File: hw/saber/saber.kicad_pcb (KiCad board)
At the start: 4 copper layers, 62.6 x 28.2 mm, 80 parts, among them J1 282834-2, J2 282834-2, J3 OSTVN12A150, J4 NUCLEO144ZE-STLINK, Q1 STL120N4F6AG, Q2 SIS413DN-T1-GE3, Q3 SSM3K337R, Q4 STL76DN4LF7AG, Q5 SSM3K337R, Q6 SSM3K337R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

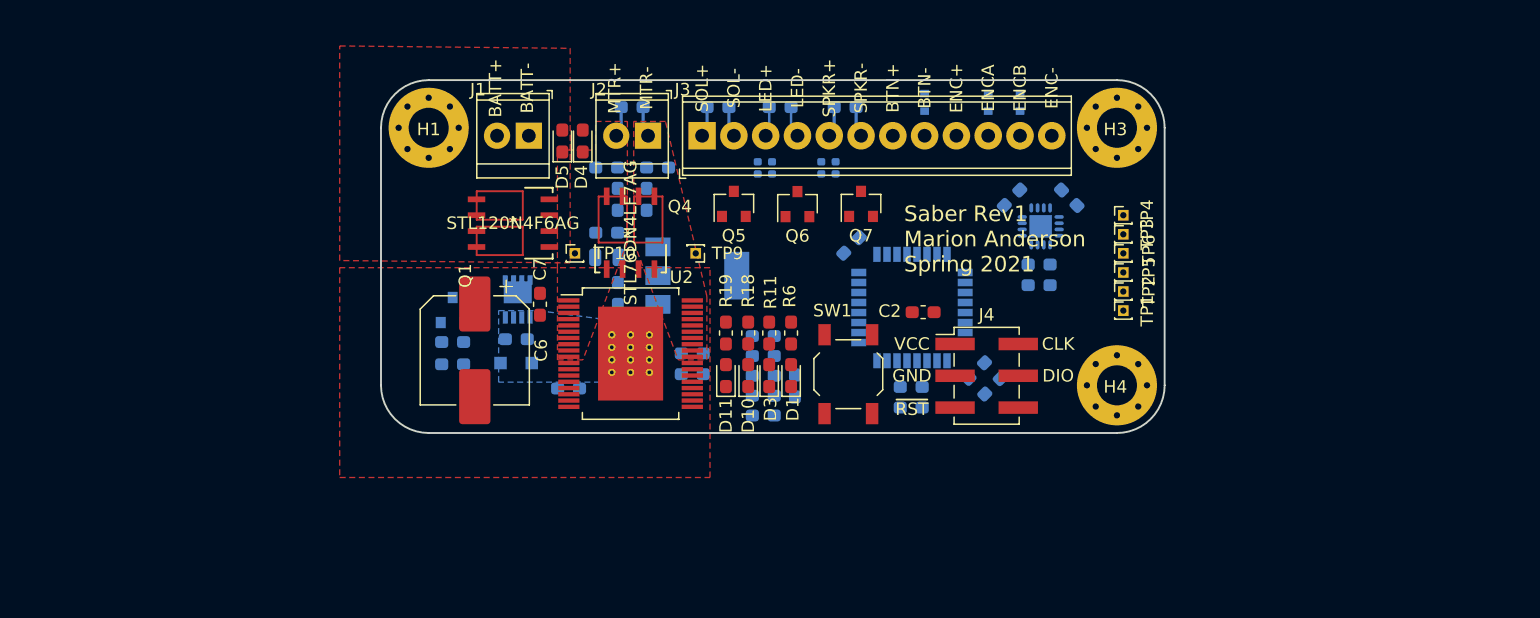
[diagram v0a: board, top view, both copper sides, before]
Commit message: more shrinking layout
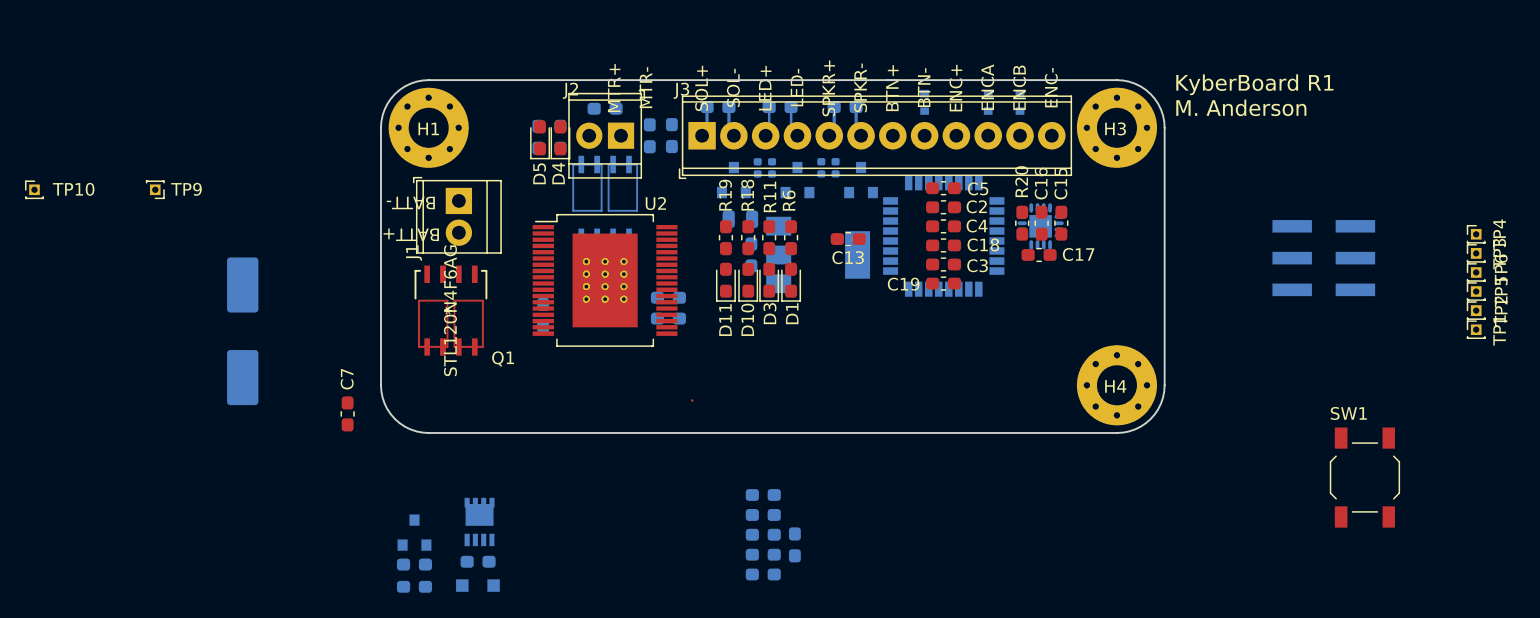
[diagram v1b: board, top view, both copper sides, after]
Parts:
- C13, C15, C16, C17, C18, C19, C3, C4, C5, R20: moved to F.Cu
- C6, J4, Q4, Q5, Q6, Q7: moved to B.Cu
- moved TP9 43.5 mm to (96.4, 76.1)
- moved TP10 43.5 mm to (86.7, 76.1)
- moved SW1 42.1 mm to (193.0, 99.1)
- moved J4 28.5 mm to (189.8, 81.5)
- moved TP1 28.2 mm to (201.9, 87.2)
- moved TP2 28.2 mm to (201.9, 85.7)
- moved TP3 28.2 mm to (201.9, 81.2)
- moved TP4 28.2 mm to (201.9, 79.6)
- moved TP5 28.2 mm to (201.9, 84.2)
- moved TP6 28.2 mm to (201.9, 82.7)
- moved C13 18.9 mm to (151.8, 80.0), turned to 180 degrees
- moved C6 18.6 mm to (103.4, 87.4), turned to 90 degrees
- moved Q2 18.0 mm to (122.3, 102.6)
- moved R10 18.0 mm to (117.1, 106.0)
- moved R9 18.0 mm to (117.1, 107.8)
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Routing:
- net /MOT-: track 2.97 -> 0.00 mm
- net /MOT+: track 2.61 -> 0.00 mm
- removed copper zone on F.Cu, net /BATT+
- removed copper zone on F.Cu, net /MOT+
- removed copper zone on F.Cu, net /MOT-
- removed copper zone on B.Cu, net /hbridge/VCC
- removed copper zone on F.Cu, net /hbridge/VCC
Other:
- board text added: "KyberBoard R1 M. Anderson"
- board text removed: "Saber Rev1 Marion Anderson Spring 2021"

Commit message: Maximum density placement. Next: Tidy for routing + minor footprint corrections
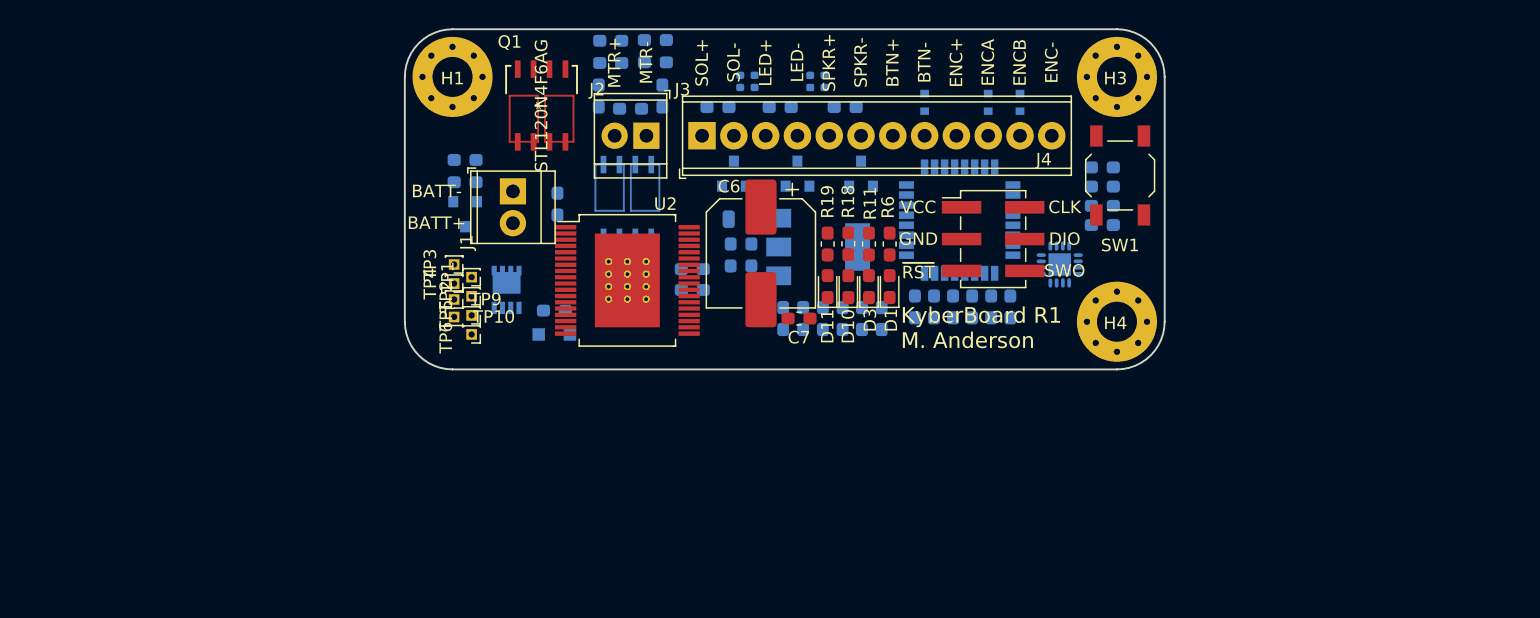
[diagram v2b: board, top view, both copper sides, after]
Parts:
- C13, C15, C16, C17, C18, C19, C2, C3, C4, C5, D4, D5, R20: moved to B.Cu
- C6, J4: moved to F.Cu
- moved TP4 81.8 mm to (120.3, 83.6), turned to 180 degrees
- moved TP3 81.7 mm to (120.3, 82.0), turned to 180 degrees
- moved TP6 80.4 mm to (121.7, 87.6), turned to 180 degrees
- moved TP1 80.4 mm to (121.7, 83.1), turned to 180 degrees
- moved TP5 80.3 mm to (121.7, 86.1), turned to 180 degrees
- moved TP2 80.3 mm to (121.7, 84.6), turned to 180 degrees
- moved C6 41.9 mm to (144.8, 81.2), turned to 270 degrees
- moved C7 36.9 mm to (147.8, 86.4), turned to 180 degrees
- moved TP10 35.0 mm to (120.3, 86.2)
- moved R9 34.3 mm to (121.1, 73.7), turned to 180 degrees
- moved SW1 31.1 mm to (173.5, 74.9), turned to 90 degrees
- moved R10 30.8 mm to (121.1, 75.5), turned to 180 degrees
- moved J4 26.5 mm to (163.3, 80.0)
- moved Q3 25.8 mm to (121.1, 78.0), turned to 270 degrees
- moved TP9 25.4 mm to (120.3, 84.8)
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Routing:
- net /LED+: track 4.02 -> 2.02 mm
- net /SPKR-: track 2.45 -> 0.56 mm
- net /SPKR+: track 4.07 -> 2.18 mm
- net /SOL-: track 2.45 -> 0.56 mm
- net +12V: track 2.45 -> 0.56 mm
- net /LED-: track 2.50 -> 0.72 mm
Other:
- board size 62.6 x 28.2 mm -> 60.7 x 27.2 mm
- board text added: "SWO"

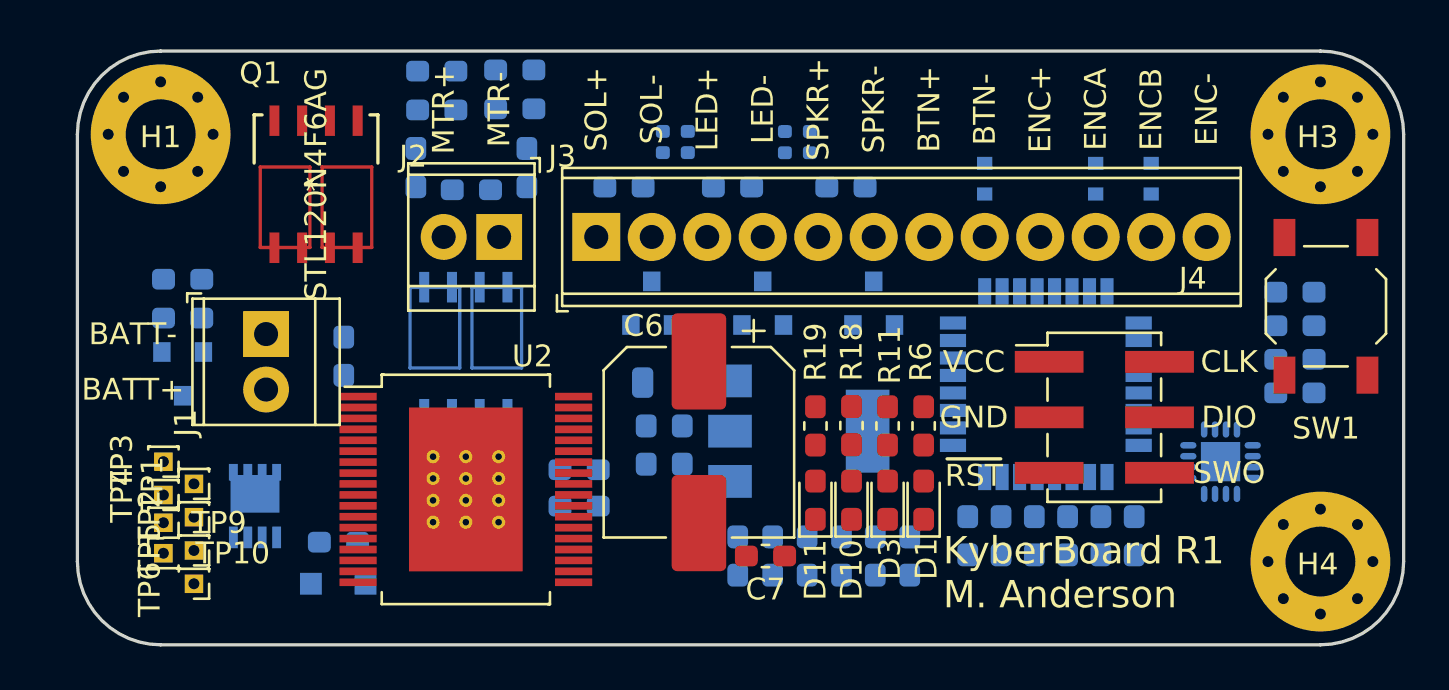
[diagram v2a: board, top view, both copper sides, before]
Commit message: correct weird pad for STL76DN4LF7AG
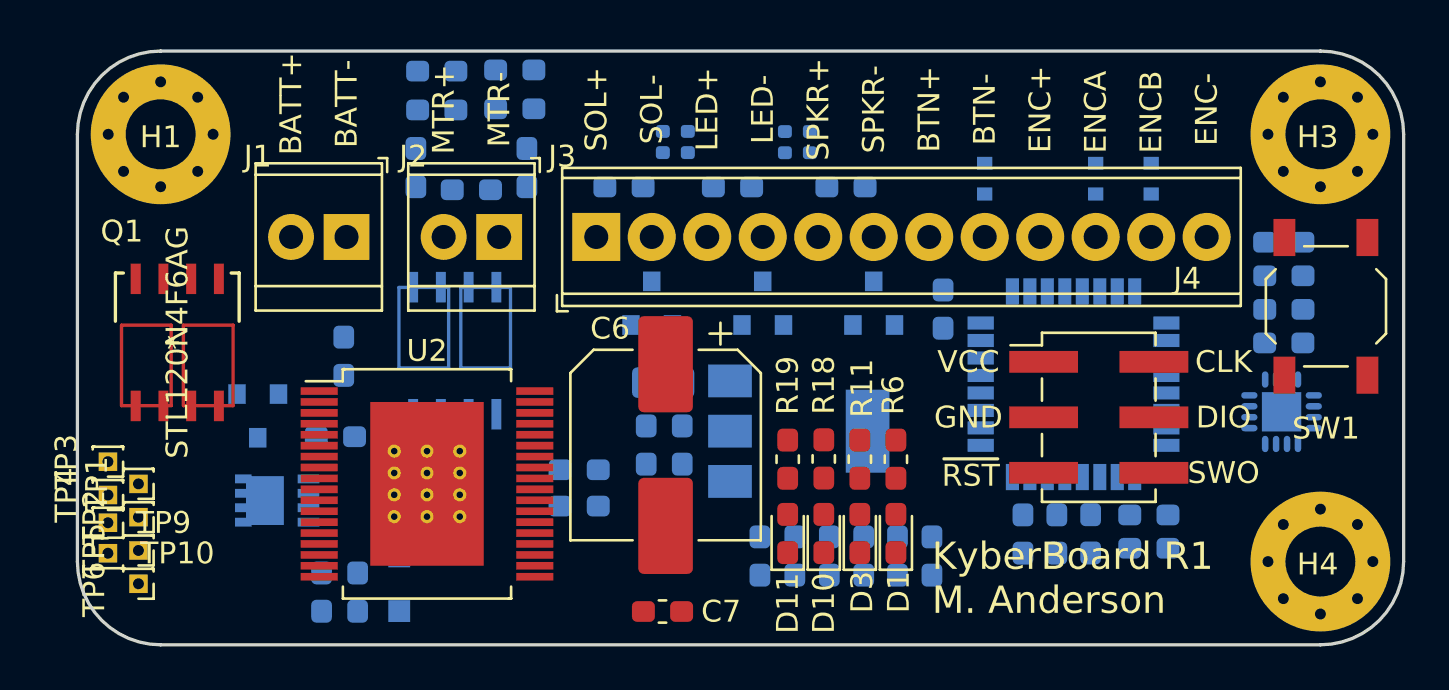
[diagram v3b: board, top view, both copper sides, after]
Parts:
- moved R9 16.4 mm to (129.2, 88.0), turned to 270 degrees
- moved R10 14.1 mm to (127.5, 88.0), turned to 90 degrees
- moved C5 13.6 mm to (156.0, 75.1), turned to 270 degrees
- moved Q1 9.63 mm to (120.9, 76.6)
- moved C3 6.83 mm to (165.4, 84.5), turned to 0 degrees
- moved J1 5.77 mm to (128.7, 71.8), turned to 180 degrees
- moved C7 5.35 mm to (143.1, 88.9)
- moved R8 4.83 mm to (128.1, 80.9)
- moved C19 4.08 mm to (161.2, 85.4), turned to 270 degrees
- moved Q3 3.94 mm to (124.6, 79.9)
- moved C4 3.76 mm to (165.4, 86.0), turned to 0 degrees
- moved U4 3.61 mm to (171.4, 79.8)
- moved D2 2.79 mm to (131.1, 87.6), turned to 270 degrees
- moved TP10 2.54 mm to (117.7, 86.2)
- moved TP3 2.54 mm to (117.7, 82.0)
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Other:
- net class Default: clearance 0.2 -> 0.13; trace_width 0.25 -> 0.2; via_dia 0.8 -> 0.5; via_drill 0.4 -> 0.254
- rule trace_clearance: 0.2 -> 0.13
- rule trace_min: 0.2 -> 0.1524
- rule via_min_drill: 0.3 -> 0.2

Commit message: pre-netlist reload commit. st transistor updated symbols + footprints
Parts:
- Q1: value STL120N4F6AG -> STL76DN4LF7AG

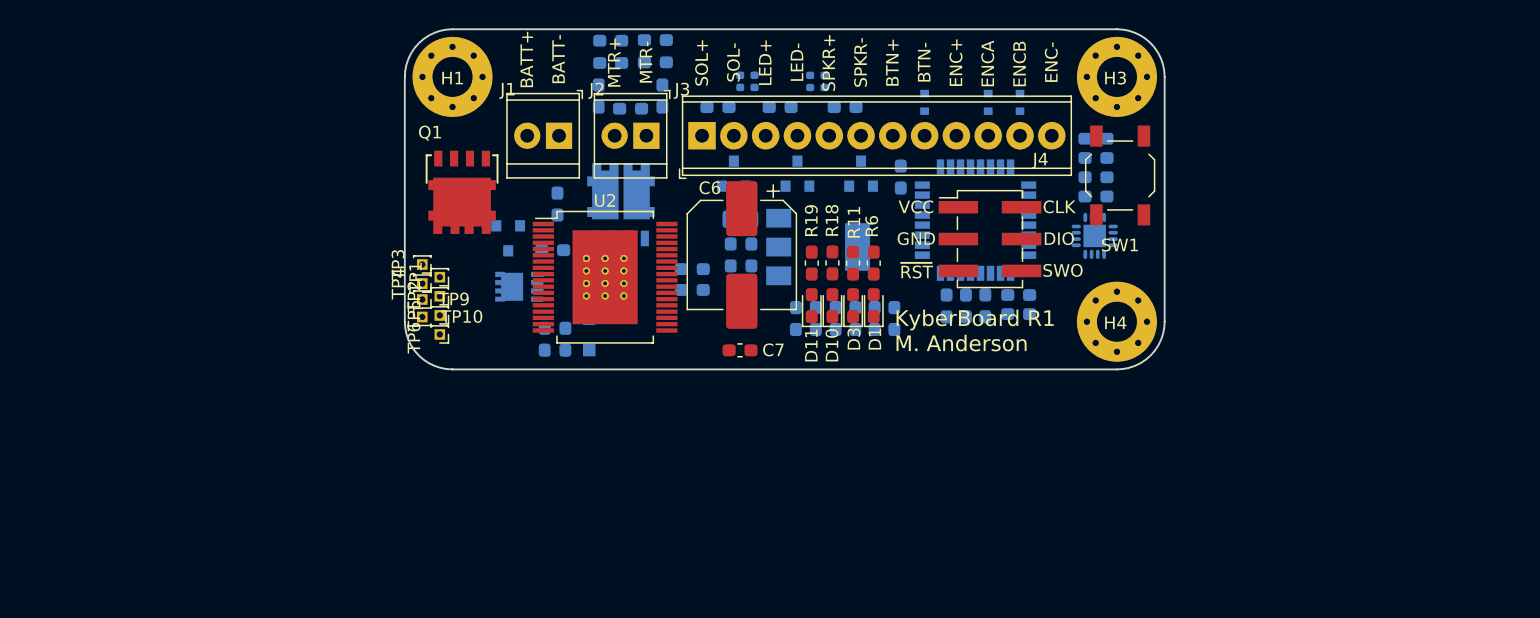
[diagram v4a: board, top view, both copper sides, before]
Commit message: power+hbridge routing round 1. fixed a transistor orientation error.
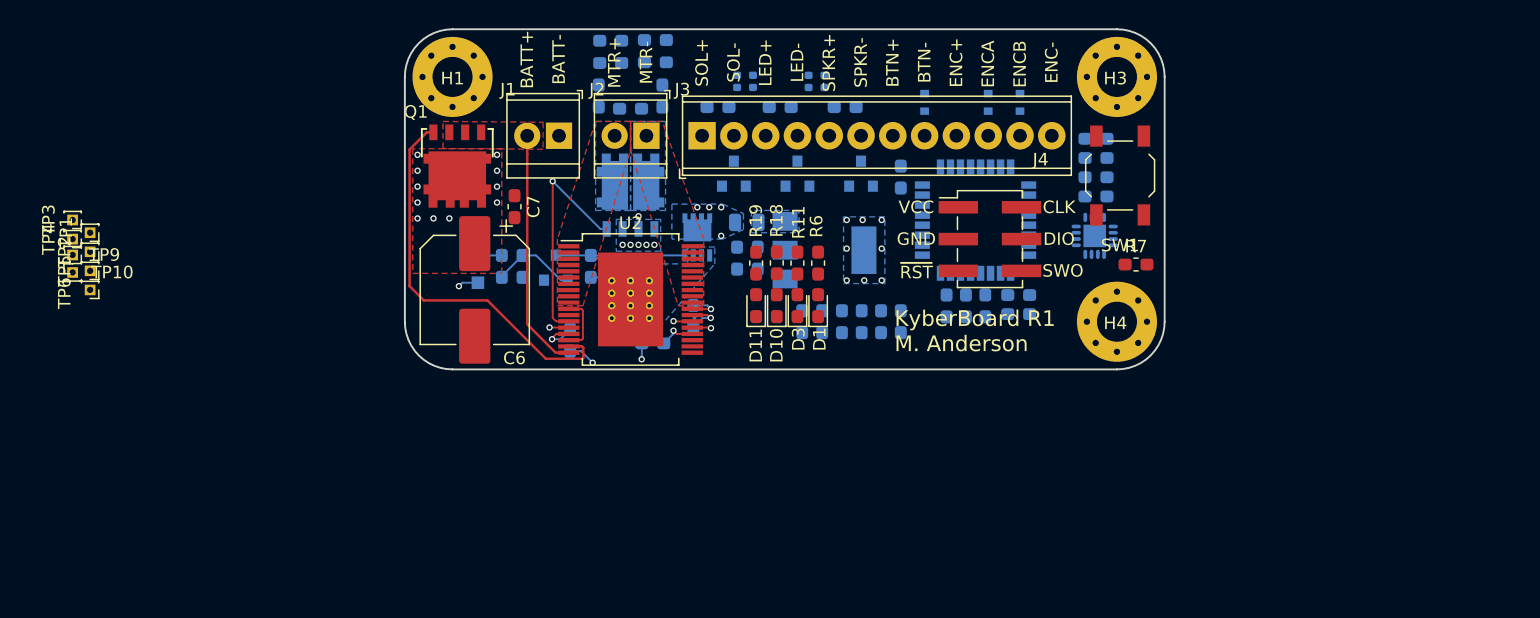
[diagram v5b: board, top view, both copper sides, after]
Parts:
- added R7: 1k, Resistor_SMD:R_0603_1608Metric_Pad1.05x0.95mm_HandSolder, F.Cu at (174.8, 82.0)
- Q1: value STL76DN4LF7AG -> STL120N4F6AG
- moved TP1 28.2 mm to (91.2, 79.5)
- moved TP10 28.2 mm to (89.8, 82.7)
- moved TP2 28.2 mm to (91.2, 81.0)
- moved TP3 28.2 mm to (89.8, 78.5)
- moved TP4 28.2 mm to (89.8, 80.0)
- moved TP5 28.2 mm to (91.2, 82.5)
- moved TP6 28.2 mm to (91.2, 84.1)
- moved TP9 28.2 mm to (89.8, 81.3)
- moved C6 21.5 mm to (121.9, 84.1)
- moved C7 21.4 mm to (125.1, 77.4), turned to 90 degrees
- moved Q2 14.8 mm to (139.7, 79.9), turned to 90 degrees
- moved R12 10.9 mm to (129.5, 88.1), turned to 270 degrees
- moved D2 10.4 mm to (122.2, 82.2), turned to 90 degrees
- moved R9 7.72 mm to (124.1, 82.2), turned to 90 degrees
- moved R10 6.08 mm to (125.7, 82.2)
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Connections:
- D3 pad 1: GND -> Net-(D3-Pad1)
- Q1 pad 1: /hbridge/VCC -> /BATT+
- Q1 pad 2: /hbridge/VCC -> /BATT+
- Q1 pad 3: /hbridge/VCC -> /BATT+
- Q1 pad 5: /BATT+ -> /hbridge/VCC
- Q2 pad 4: Net-(Q2-Pad4) -> Net-(D3-Pad1)
- Q3 pad 3: Net-(Q2-Pad4) -> Net-(D3-Pad1)
- R11 pad 1: Net-(Q2-Pad4) -> /hbridge/VCC
- R8 pad 2: Net-(Q2-Pad4) -> Net-(D3-Pad1)
- SW1 pad 2: GND -> Net-(R7-Pad1)
- TP10 pad 1: Net-(Q4-Pad2) -> Net-(Q4-Pad4)
- TP9 pad 1: Net-(Q4-Pad4) -> Net-(Q4-Pad2)
- U2 pad 13: Net-(Q4-Pad2) -> Net-(Q4-Pad4)
- U2 pad 24: Net-(Q4-Pad4) -> Net-(Q4-Pad2)
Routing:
- net Net-(Q1-Pad4): track 0.00 -> 31.7 mm
- net /BATT+: track 0.00 -> 19.3 mm
- net Net-(Q4-Pad4): track 0.00 -> 18.2 mm, vias 0 -> 1
- net Net-(Q4-Pad2): track 0.00 -> 13.7 mm, vias 0 -> 2
- net Net-(D3-Pad1): track 0.00 -> 10.7 mm
- net GND: track 0.00 -> 9.55 mm, vias 0 -> 10
- net Net-(Q3-Pad1): track 0.00 -> 6.87 mm
- net /hbridge/INA: track 0.00 -> 4.61 mm
- net Net-(C8-Pad1): track 0.00 -> 3.44 mm, vias 0 -> 1
- net Net-(R12-Pad1): track 0.00 -> 3.34 mm, vias 0 -> 1
- net /hbridge/VCC: track 0.00 -> 3.02 mm, vias 0 -> 12
- net Net-(R13-Pad1): track 0.00 -> 2.95 mm, vias 0 -> 1
- net Net-(D2-Pad2): track 0.00 -> 2.04 mm
- net +3V3: vias 0 -> 8
- net +12V: vias 0 -> 4
- added copper zone on B.Cu, net +12C
- added copper zone on B.Cu, net +12V
- added copper zone on B.Cu, net +3V3
- added copper zone on F.Cu, net /BATT+
- added copper zone on B.Cu, net /MOT+
- added copper zone on F.Cu, net /MOT+
- added copper zone on B.Cu, net /MOT-
- added copper zone on F.Cu, net /MOT-
- added copper zone on B.Cu, net /hbridge/VCC
- added copper zone on F.Cu, net /hbridge/VCC
- added copper zone on In1.Cu, net /hbridge/VCC
- added copper zone on B.Cu, net GND
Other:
- net class Default: clearance 0.13 -> 0.2032; via_dia 0.5 -> 0.508; via_drill 0.254 -> 0.29972
- rule trace_clearance: 0.13 -> 0.2032

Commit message: starting signal routing
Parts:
- removed TP1, TP10, TP2, TP3, TP4, TP5, TP6, TP9: TestPoint, Connector_PinHeader_1.00mm:PinHeader_1x01_P1.00mm_Vertical
- moved D11 3.94 mm to (148.3, 85.3)
- moved R19 3.94 mm to (148.3, 81.9)
- moved D3 2.67 mm to (145.0, 85.3)
- moved R11 2.67 mm to (145.0, 81.9)
- moved R7 1.14 mm to (175.4, 81.1), turned to 270 degrees
- moved C7 0.99 mm to (126.0, 77.0), turned to 0 degrees
- moved D1 0.63 mm to (150.0, 85.3)
- moved D10 0.63 mm to (146.7, 85.3)
- moved R18 0.63 mm to (146.7, 81.9)
- moved R6 0.63 mm to (150.0, 81.9)
- moved C1 0.18 mm to (153.0, 86.5)
- moved R2 0.18 mm to (156.1, 86.5)
- moved R3 0.18 mm to (148.2, 86.5)
- moved R5 0.18 mm to (154.5, 86.5)
- moved R1 0.18 mm to (149.8, 86.5)
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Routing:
- net GND: track 9.55 -> 42.5 mm, vias 10 -> 17
- net /hbridge/INA: track 4.61 -> 32.2 mm, vias 0 -> 1
- net Net-(D3-Pad1): track 10.7 -> 24.0 mm, vias 0 -> 1
- net +3V3: track 0.00 -> 13.0 mm, vias 8 -> 9
- net /hbridge/imtr: track 0.00 -> 12.8 mm
- net /hbridge/PWM_MTR: track 0.00 -> 11.0 mm, vias 0 -> 1
- net /hbridge/INB: track 0.00 -> 9.21 mm, vias 0 -> 1
- net /micro/LED_HBEAT: track 0.00 -> 8.27 mm
- net +12C: track 0.00 -> 3.04 mm
- net Net-(R7-Pad1): track 0.00 -> 2.14 mm
- net Net-(D10-Pad2): track 0.00 -> 1.66 mm
- net Net-(D3-Pad2): track 0.00 -> 1.65 mm
- net Net-(D11-Pad2): track 0.00 -> 1.65 mm
- net Net-(D1-Pad2): track 0.00 -> 1.65 mm
- net /hbridge/VCC: track 3.02 -> 2.69 mm, vias 12 -> 3
- added copper zone on F.Cu, net GND
